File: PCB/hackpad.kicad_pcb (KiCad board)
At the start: 2 copper layers, 93.1 x 73.4 mm, 28 parts, among them J1 OLED_DISPLAY, SW1 SW_Push, SW2 SW_Push, SW3 SW_Push, SW4 SW_Push, SW5 SW_Push, SW6 SW_Push, SW7 SW_Push, SW8 SW_Push, SW9 RotaryEncoder_Switch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

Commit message: uploading stuff
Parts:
- moved J1 5.12 mm to (138.7, 75.0), turned to 0 degrees
- moved D9 3.48 mm to (136.8, 89.2)
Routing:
- net Net-(J1-Pin_4): track 18.0 -> 33.9 mm
- net GND: track 383.5 -> 373.5 mm
- net Net-(J1-Pin_3): track 21.6 -> 29.6 mm
- net /COL4: track 142.9 -> 150.3 mm
- net +3.3V: track 39.7 -> 45.8 mm
- net Net-(D9-A): track 14.7 -> 16.2 mm

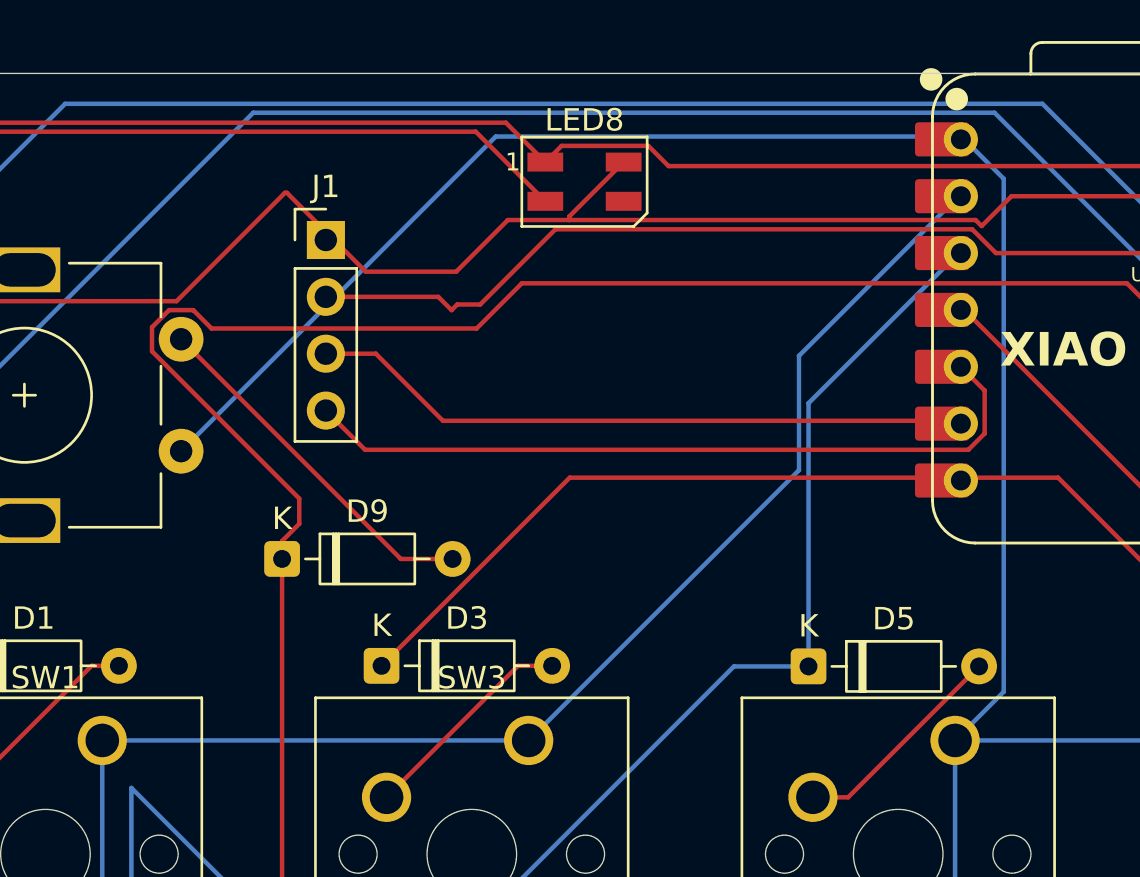
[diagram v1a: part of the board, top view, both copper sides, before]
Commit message: uploading files
clearing drc
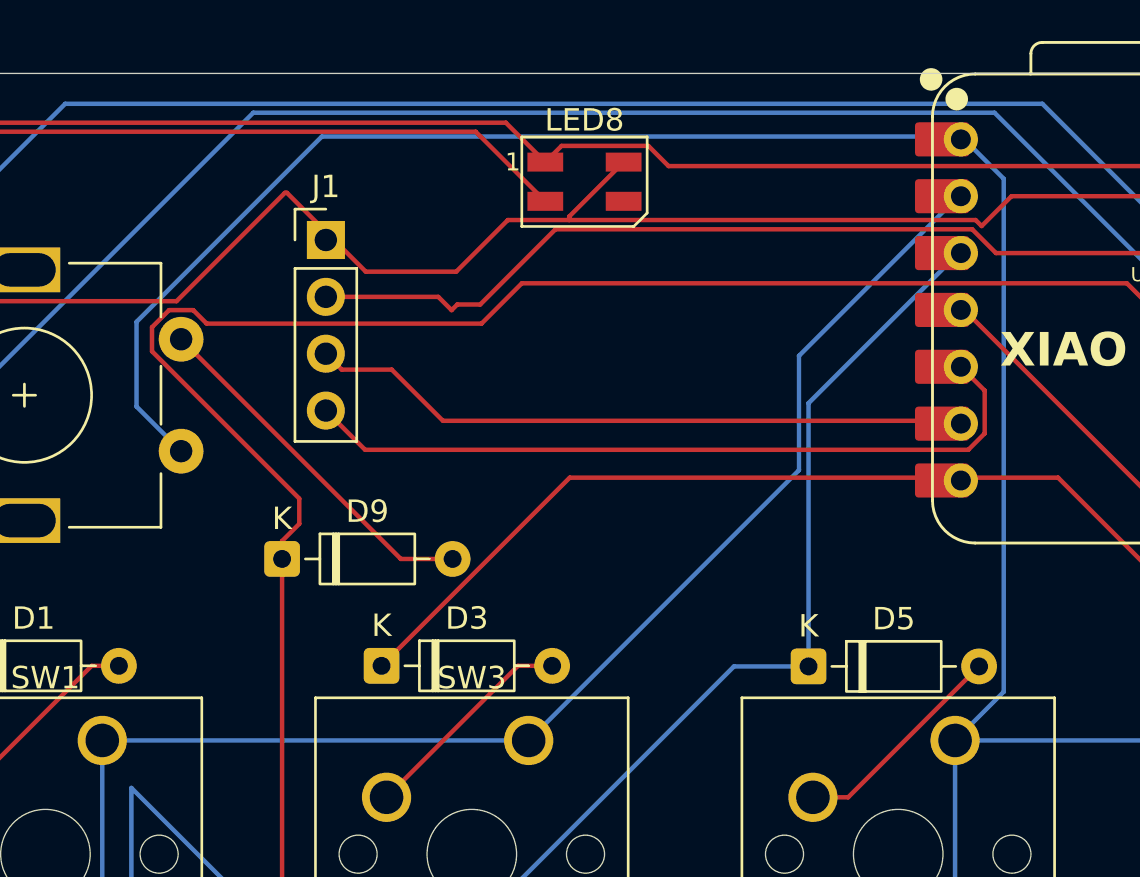
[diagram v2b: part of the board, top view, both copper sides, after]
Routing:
- net /ROW2: track 126.8 -> 133.0 mm
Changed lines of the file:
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@@
+	)
+	(segment
+		(start 136.779 125.9205)
+		(end 136.779 89.2048)
+		(width 0.2)
+		(layer "F.Cu")
+		(net 7)
+	)
+	(segment
+		(start 136.779 88.4048)
+		(end 136.779 89.2048)
+		(width 0.2)
+		(layer "F.Cu")
+		(net 7)
+	)
+	(segment
+		(start 136.68375 126.01575)
+		(end 140.6398 129.9718)
+		(width 0.2)
+		(layer "F.Cu")
+		(net 7)
+	)
+	(segment
+		(start 137.5474 86.508092)
+		(end 137.5474 87.6364)
+		(width 0.2)
+		(layer "F.Cu")
+		(net 7)
+	)
+	(segment
+		(start 133.408292 78.6892)
+		(end 132.807692 78.0886)
+		(width 0.2)
+		(layer "F.Cu")
+		(net 7)
+	)
+	(segment
+		(start 174.524 76.8896)
+		(end 147.49184 76.8896)
+		(width 0.2)
+		(layer "F.Cu")
+		(net 7)
+	)
+	(segment
+		(start 136.68375 126.01575)
+		(end 136.779 125.9205)
+		(width 0.2)
+		(layer "F.Cu")
+		(net 7)
+	)
+	(segment
+		(start 145.69224 78.6892)
+		(end 133.408292 78.6892)
+		(width 0.2)
+		(layer "F.Cu")
+		(net 7)
+	)
+	(segment
+		(start 174.879 127.9906)
+		(end 176.3268 129.4384)
+		(width 0.2)
+		(layer "F.Cu")
+		(net 7)
+	)
+	(segment
+		(start 132.807692 78.0886)
+		(end 131.729908 78.0886)
+		(width 0.2)
+		(layer "F.Cu")
+		(net 7)
+	)
+	(segment
+		(start 131.729908 78.0886)
+		(end 130.9678 78.850708)
+		(width 0.2)
+		(layer "F.Cu")
+		(net 7)
+	)
+	(segment
+		(start 147.49184 76.8896)
+		(end 145.69224 78.6892)
+		(width 0.2)
+		(layer "F.Cu")
+		(net 7)
+	)
+	(segment
+		(start 140.6398 129.9718)
+		(end 142.621 127.9906)
+		(width 0.2)
+		(layer "F.Cu")
+		(net 7)
 	)
 	(segment
@@
 	)
 	(segment
-		(start 136.779 125.9205)
-		(end 136.779 89.2048)
-		(width 0.2)
-		(layer "F.Cu")
-		(net 7)
-	)
-	(segment
-		(start 136.68375 126.01575)
-		(end 140.6398 129.9718)
-		(width 0.2)
-		(layer "F.Cu")
-		(net 7)
-	)
-	(segment
-		(start 137.5474 86.508092)
-		(end 137.5474 87.6364)
-		(width 0.2)
-		(layer "F.Cu")
-		(net 7)
-	)
-	(segment
-		(start 147.49184 76.8896)
-		(end 145.47164 78.9098)
+		(start 183.207 85.5726)
+		(end 174.524 76.8896)
+		(width 0.2)
+		(layer "F.Cu")
+		(net 7)
+	)
+	(segment
+		(start 137.5474 87.6364)
+		(end 136.779 88.4048)
 		(width 0.2)
 		(layer "F.Cu")
@@
 	)
 	(segment
-		(start 131.729908 78.0886)
-		(end 130.9678 78.850708)
-		(width 0.2)
-		(layer "F.Cu")
-		(net 7)
-	)
-	(segment
-		(start 132.807692 78.0886)
-		(end 131.729908 78.0886)
-		(width 0.2)
-		(layer "F.Cu")
-		(net 7)
-	)
-	(segment
-		(start 136.779 88.4048)
-		(end 136.779 89.2048)
-		(width 0.2)
-		(layer "F.Cu")
-		(net 7)
-	)
-	(segment
-		(start 136.68375 126.01575)
-		(end 136.779 125.9205)
-		(width 0.2)
-		(layer "F.Cu")
-		(net 7)
-	)
-	(segment
-		(start 174.879 127.9906)
-		(end 176.3268 129.4384)
-		(width 0.2)
-		(layer "F.Cu")
-		(net 7)
-	)
-	(segment
-		(start 174.524 76.8896)
-		(end 147.49184 76.8896)
-		(width 0.2)
-		(layer "F.Cu")
-		(net 7)
-	)
-	(segment
-		(start 133.628892 78.9098)
-		(end 132.807692 78.0886)
-		(width 0.2)
-		(layer "F.Cu")
-		(net 7)
-	)
-	(segment
-		(start 137.5474 87.6364)
-		(end 136.779 88.4048)
-		(width 0.2)
-		(layer "F.Cu")
-		(net 7)
-	)
-	(segment
-		(start 140.6398 129.9718)
-		(end 142.621 127.9906)
-		(width 0.2)
-		(layer "F.Cu")
-		(net 7)
-	)
-	(segment
-		(start 145.47164 78.9098)
-		(end 133.628892 78.9098)
-		(width 0.2)
-		(layer "F.Cu")
-		(net 7)
-	)
-	(segment
-		(start 183.207 85.5726)
-		(end 174.524 76.8896)
-		(width 0.2)
-		(layer "F.Cu")
-		(net 7)
-	)
-	(segment
 		(start 142.621 127.9906)
 		(end 174.879 127.9906)
@@
 	)
 	(segment
-		(start 167.132 70.3326)
-		(end 169.0204 72.221)
+		(start 169.0204 72.221)
+		(end 167.132 70.3326)
 		(width 0.2)
 		(layer "B.Cu")
@@
 	)
 	(segment
+		(start 169.0204 95.1396)
+		(end 169.0204 72.221)
+		(width 0.2)
+		(layer "B.Cu")
+		(net 23)
+	)
+	(segment
 		(start 167.132 70.3326)
-		(end 146.3258 70.3326)
+		(end 138.557 70.3326)
+		(width 0.2)
+		(layer "B.Cu")
+		(net 23)
+	)
+	(segment
+		(start 166.84625 97.31375)
+		(end 169.0204 95.1396)
+		(width 0.2)
+		(layer "B.Cu")
+		(net 23)
+	)
+	(segment
+		(start 130.2766 78.613)
+		(end 130.2766 82.3974)
 		(width 0.2)
 		(layer "B.Cu")
@@
 	)
 	(segment
-		(start 169.0204 72.221)
-		(end 169.0204 95.1396)
-		(width 0.2)
-		(layer "B.Cu")
-		(net 23)
-	)
-	(segment
 		(start 167.72255 116.36375)
 		(end 185.89625 116.36375)
@@
 	)
 	(segment
-		(start 146.3258 70.3326)
+		(start 130.2766 82.3974)
 		(end 132.2688 84.3896)
 		(width 0.2)
@@
 	)
 	(segment
-		(start 169.0204 95.1396)
-		(end 166.84625 97.31375)
+		(start 138.557 70.3326)
+		(end 130.2766 78.613)
 		(width 0.2)
 		(layer "B.Cu")
@@
 	)
 	(segment
-		(start 143.9672 83.0326)
-		(end 140.97 80.0354)
+		(start 139.446 80.7466)
+		(end 138.7348 80.0354)
 		(width 0.2)
 		(layer "F.Cu")
@@
 	)
 	(segment
-		(start 140.97 80.0354)
-		(end 138.7348 80.0354)
-		(width 0.2)
-		(layer "F.Cu")
+		(start 141.6812 80.7466)
+		(end 139.446 80.7466)
+		(width 0.2)
+		(layer "F.Cu")
+		(net 27)
+	)
+	(segment
+		(start 143.9672 83.0326)
+		(end 141.6812 80.7466)
+		(width 0.2)
+		(layer "F.Cu")
